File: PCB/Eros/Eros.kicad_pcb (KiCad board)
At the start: 4 copper layers, 65 x 71 mm, 114 parts, among them IC1 ADS1292RIPBS, J1 USB_C_PowerOnly_6P, J2 UART, J3 Li-ion, J4 Conn_01x08_Socket, J5 AudioJack3, J6 Micro_SD_Card, J7 Conn_01x03_Socket, Q1 BC817, SW1 SW_Push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

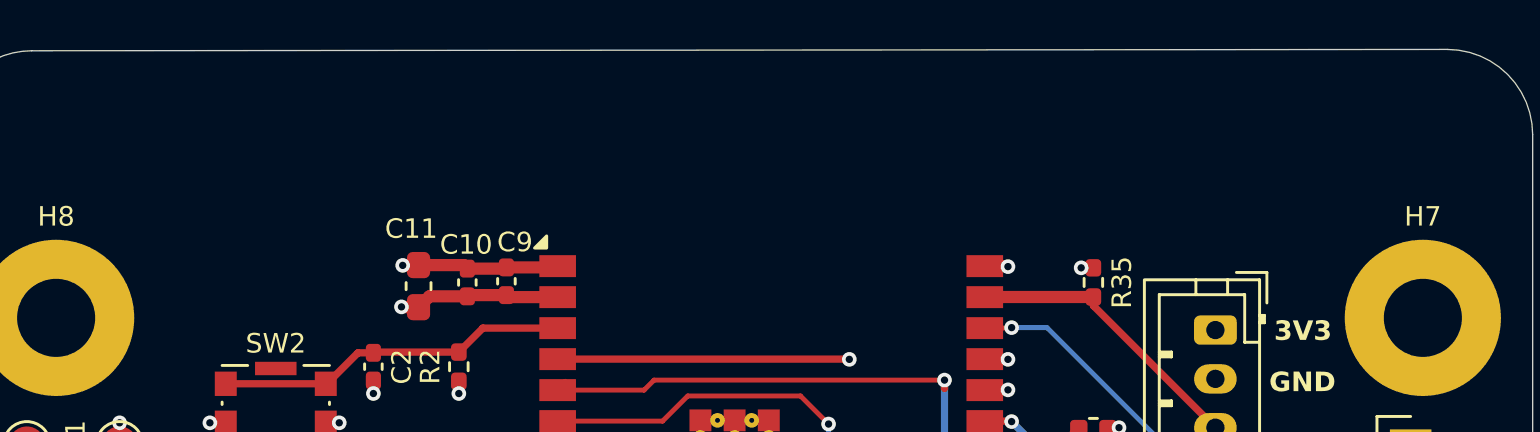
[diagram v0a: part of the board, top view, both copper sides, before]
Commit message: update vias
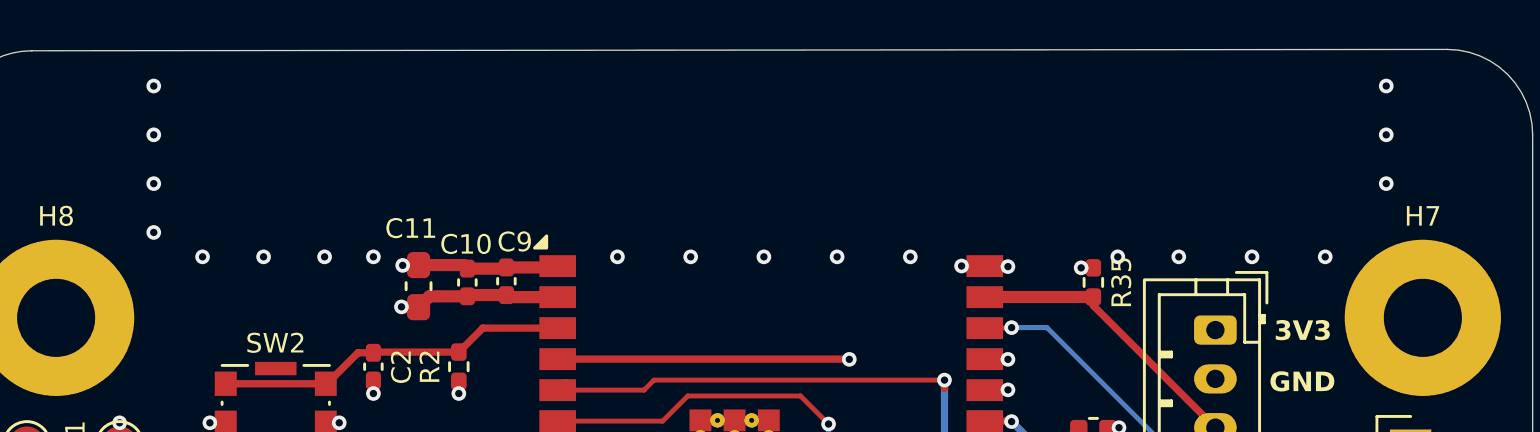
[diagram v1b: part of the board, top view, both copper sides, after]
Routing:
- net GND: track 83.8 -> 84.7 mm, vias 56 -> 77
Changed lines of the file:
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@@
+	)
+	(segment
+		(start 195.05 58.38)
+		(end 194.105 58.38)
+		(width 0.5)
+		(layer "F.Cu")
+		(net 86)
 	)
 	(segment
@@
 	)
 	(segment
+		(start 194.105 58.38)
+		(end 194.1 58.375)
+		(width 0.5)
+		(layer "F.Cu")
+		(net 86)
+	)
+	(segment
 		(start 173.85 58.4825)
 		(end 175.4 58.4825)
@@
 	)
 	(via
+		(at 161 53)
+		(size 0.6)
+		(drill 0.3)
+		(layers "F.Cu" "B.Cu")
+		(free yes)
+		(net 86)
+	)
+	(via
 		(at 181.95 93.4)
 		(size 0.6)
@@
 	)
 	(via
+		(at 194.1 58.375)
+		(size 0.6)
+		(drill 0.3)
+		(layers "F.Cu" "B.Cu")
+		(net 86)
+	)
+	(via
 		(at 206.75 80.2)
 		(size 0.6)
@@
 	)
 	(via
+		(at 189 58)
+		(size 0.6)
+		(drill 0.3)
+		(layers "F.Cu" "B.Cu")
+		(free yes)
+		(net 86)
+	)
+	(via
 		(at 201.3 83)
 		(size 0.6)
@@
 	)
 	(via
+		(at 209 58)
+		(size 0.6)
+		(drill 0.3)
+		(layers "F.Cu" "B.Cu")
+		(free yes)
+		(net 86)
+	)
+	(via
 		(at 192.65 87.65)
 		(size 0.6)
@@
 	)
 	(via
+		(at 161 51)
+		(size 0.6)
+		(drill 0.3)
+		(layers "F.Cu" "B.Cu")
+		(free yes)
+		(net 86)
+	)
+	(via
 		(at 189.9 106.1)
 		(size 0.6)
@@
 	)
 	(via
+		(at 168 58)
+		(size 0.6)
+		(drill 0.3)
+		(layers "F.Cu" "B.Cu")
+		(free yes)
+		(net 86)
+	)
+	(via
 		(at 202.5 85.15)
 		(size 0.6)
@@
 	)
 	(via
+		(at 161 57)
+		(size 0.6)
+		(drill 0.3)
+		(layers "F.Cu" "B.Cu")
+		(free yes)
+		(net 86)
+	)
+	(via
 		(at 188.75 83.55)
 		(size 0.6)
@@
 	)
 	(via
+		(at 200.5 58)
+		(size 0.6)
+		(drill 0.3)
+		(layers "F.Cu" "B.Cu")
+		(free yes)
+		(net 86)
+	)
+	(via
 		(at 165.05 85.95)
 		(size 0.6)
@@
 	)
 	(via
+		(at 180 58)
+		(size 0.6)
+		(drill 0.3)
+		(layers "F.Cu" "B.Cu")
+		(free yes)
+		(net 86)
+	)
+	(via
 		(at 159.6 64.8)
 		(size 0.6)
@@
 	)
 	(via
+		(at 183 58)
+		(size 0.6)
+		(drill 0.3)
+		(layers "F.Cu" "B.Cu")
+		(free yes)
+		(net 86)
+	)
+	(via
 		(at 202.05 80.85)
 		(size 0.6)
@@
 	)
 	(via
+		(at 203 58)
+		(size 0.6)
+		(drill 0.3)
+		(layers "F.Cu" "B.Cu")
+		(free yes)
+		(net 86)
+	)
+	(via
 		(at 207.95 82.95)
 		(size 0.6)
@@
 	)
 	(via
+		(at 211.5 51)
+		(size 0.6)
+		(drill 0.3)
+		(layers "F.Cu" "B.Cu")
+		(free yes)
+		(net 86)
+	)
+	(via
 		(at 196 58.4)
 		(size 0.6)
@@
 	)
 	(via
+		(at 192 58)
+		(size 0.6)
+		(drill 0.3)
+		(layers "F.Cu" "B.Cu")
+		(free yes)
+		(net 86)
+	)
+	(via
 		(at 176.5 89.25)
 		(size 0.6)
@@
 	)
 	(via
+		(at 163 58)
+		(size 0.6)
+		(drill 0.3)
+		(layers "F.Cu" "B.Cu")
+		(free yes)
+		(net 86)
+	)
+	(via
 		(at 206.8 88.6)
 		(size 0.6)
@@
 	)
 	(via
+		(at 211.5 53)
+		(size 0.6)
+		(drill 0.3)
+		(layers "F.Cu" "B.Cu")
+		(free yes)
+		(net 86)
+	)
+	(via
 		(at 213.6 111.95)
 		(size 0.6)
@@
 	)
 	(via
+		(at 170 58)
+		(size 0.6)
+		(drill 0.3)
+		(layers "F.Cu" "B.Cu")
+		(free yes)
+		(net 86)
+	)
+	(via
+		(at 206 58)
+		(size 0.6)
+		(drill 0.3)
+		(layers "F.Cu" "B.Cu")
+		(free yes)
+		(net 86)
+	)
+	(via
+		(at 186 58)
+		(size 0.6)
+		(drill 0.3)
+		(layers "F.Cu" "B.Cu")
+		(free yes)
+		(net 86)
+	)
+	(via
+		(at 211.5 55)
+		(size 0.6)
+		(drill 0.3)
+		(layers "F.Cu" "B.Cu")
+		(free yes)
+		(net 86)
+	)
+	(via
 		(at 181.95 94.55)
 		(size 0.6)
@@
 	)
 	(via
+		(at 161 55)
+		(size 0.6)
+		(drill 0.3)
+		(layers "F.Cu" "B.Cu")
+		(free yes)
+		(net 86)
+	)
+	(via
 		(at 196 82.05)
 		(size 0.6)
@@
 		(net 86)
 	)
+	(via
+		(at 165.5 58)
+		(size 0.6)
+		(drill 0.3)
+		(layers "F.Cu" "B.Cu")
+		(free yes)
+		(net 86)
+	)
